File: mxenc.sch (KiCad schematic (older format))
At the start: 28 parts, among them J4 Conn_01x06, J6 Conn_01x06, J8 Conn_01x06 DNP, SW1 SW_Push, SW2 SW_Push, U1 IMX8MM, U10 24LC16, Y2 Crystal_GND24

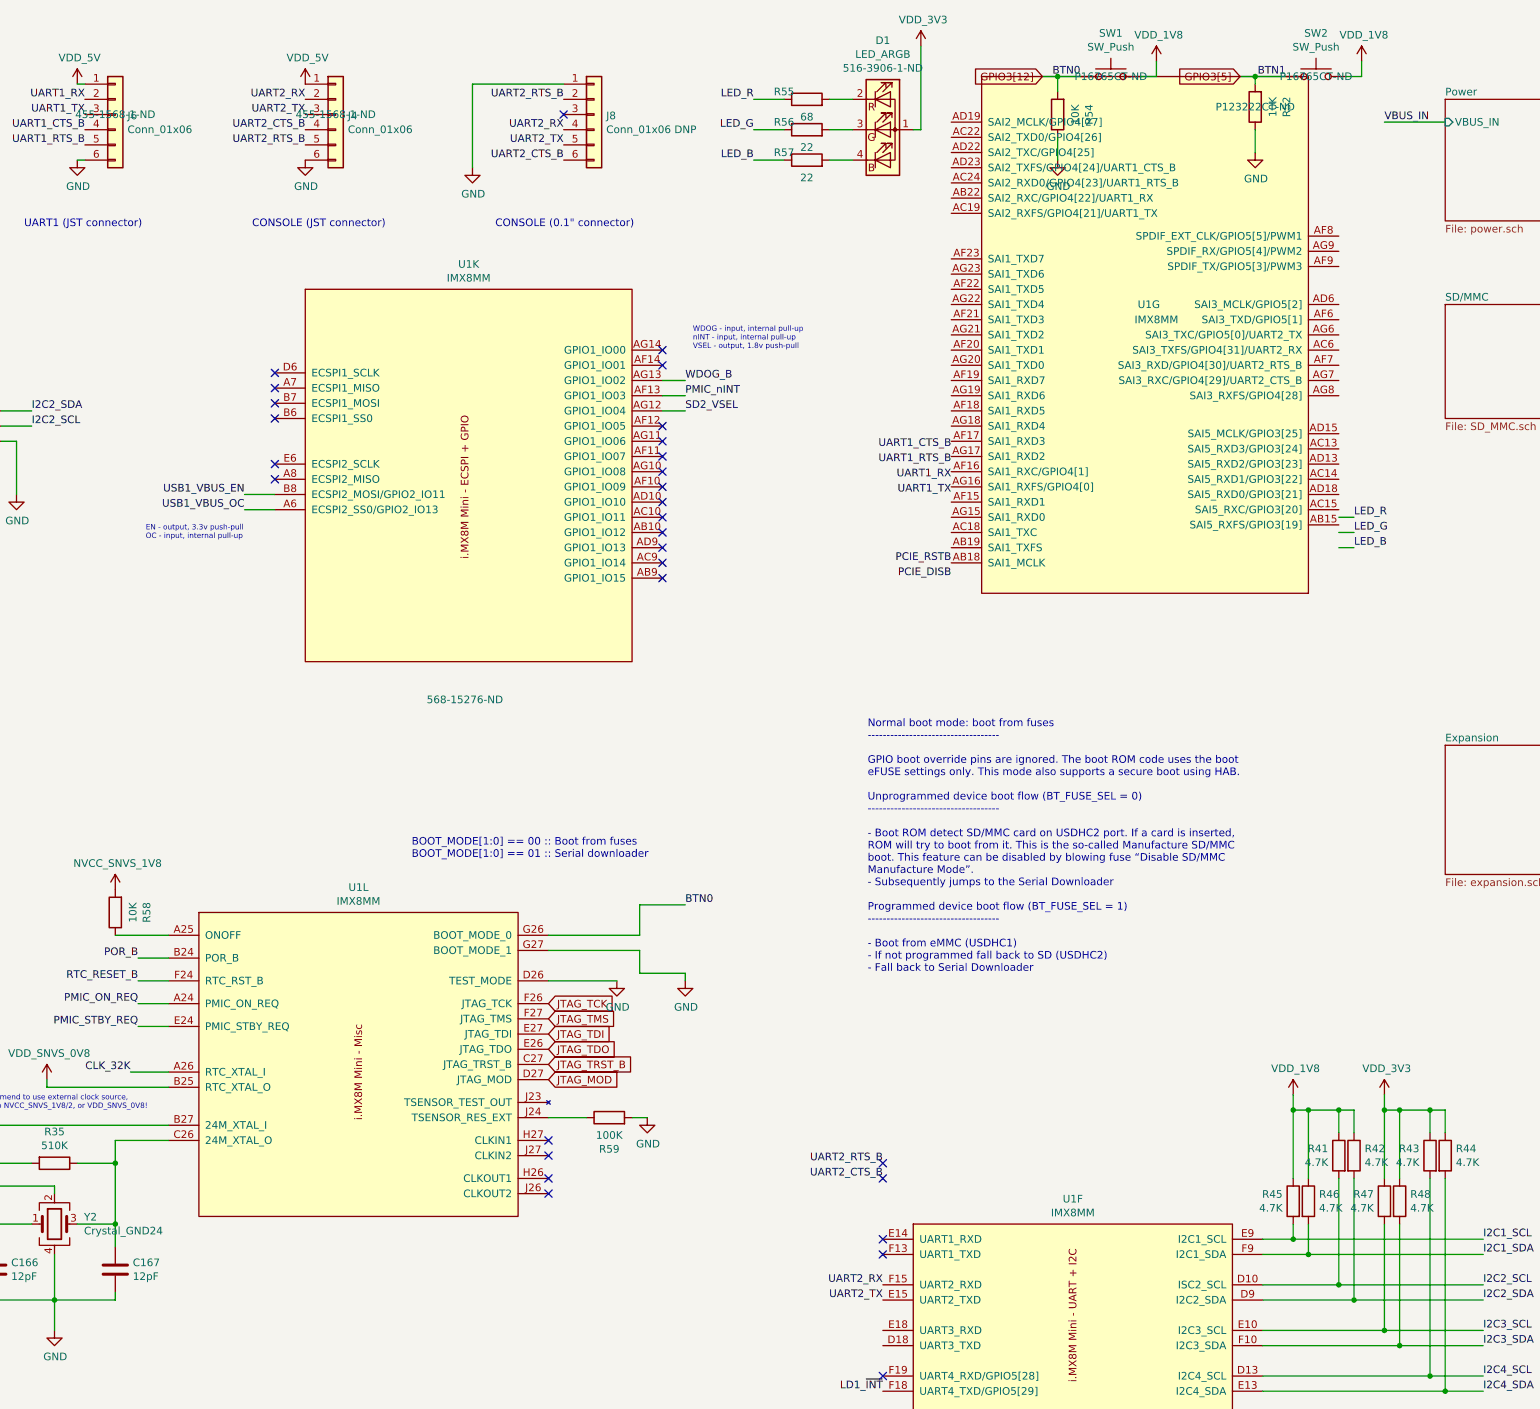
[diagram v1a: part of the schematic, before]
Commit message: add sai, mdio, sdhc to headers
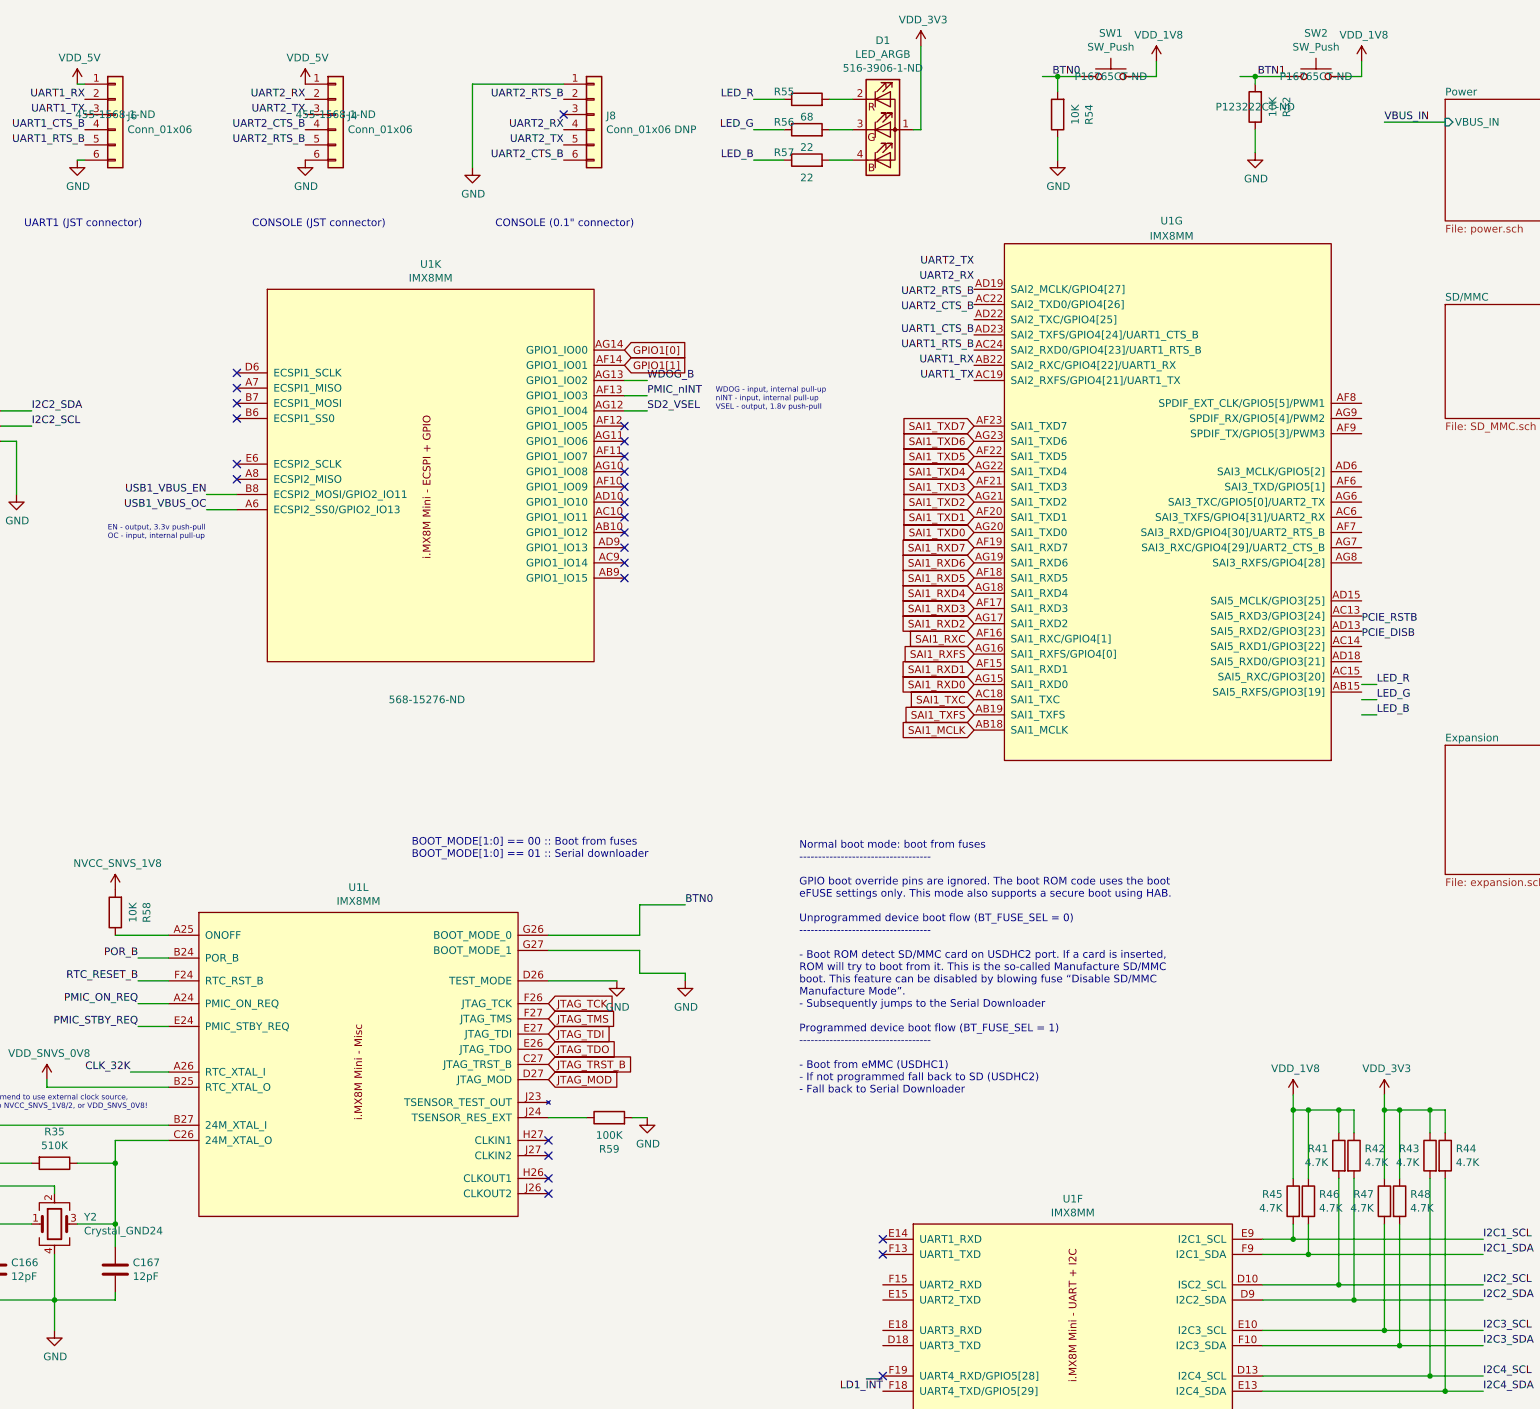
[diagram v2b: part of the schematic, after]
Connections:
- net labels added: GPIO1[0], GPIO1[1], SAI1_MCLK, SAI1_RXC, SAI1_RXD0, SAI1_RXD1, SAI1_RXD2, SAI1_RXD3, SAI1_RXD4, SAI1_RXD5, SAI1_RXD6, SAI1_RXD7, SAI1_RXFS, SAI1_TXC, SAI1_TXD0, SAI1_TXD1, SAI1_TXD2, SAI1_TXD3, SAI1_TXD4, SAI1_TXD5, SAI1_TXD6, SAI1_TXD7, SAI1_TXFS
- net labels removed: GPIO3[12], GPIO3[5]
- no-connect marks 32 -> 28
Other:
- moved on the sheet: U1G, U1K
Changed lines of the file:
@@
 L mxenc:MIMX8MM6DVTLZAA U1
 U 11 1 5DDE75DF
-P 4550 5250
-F 0 "U1" H 4575 8115 50  0000 C CNN
-F 1 "IMX8MM" H 4575 8024 50  0000 C CNN
-F 2 "mxenc:BGA-729_27x27_14.0x14.0mm" H 4800 8000 50  0001 C CNN
-F 3 "" H 3800 8000 50  0001 C CNN
-F 4 "568-15276-ND" H 4550 5250 50  0000 C CNN "Vendorpart"
-F 5 "NXP" H 4550 5250 50  0001 C CNN "Mfgr"
-F 6 "MIMX8MM6CVTKZAA" H 4550 5250 50  0001 C CNN "Part"
-	11   4550 5250
+P 4300 5250
+F 0 "U1" H 4325 8115 50  0000 C CNN
+F 1 "IMX8MM" H 4325 8024 50  0000 C CNN
+F 2 "mxenc:BGA-729_27x27_14.0x14.0mm" H 4550 8000 50  0001 C CNN
+F 3 "" H 3550 8000 50  0001 C CNN
+F 4 "568-15276-ND" H 4300 5250 50  0000 C CNN "Vendorpart"
+F 5 "NXP" H 4300 5250 50  0001 C CNN "Mfgr"
+F 6 "MIMX8MM6CVTKZAA" H 4300 5250 50  0001 C CNN "Part"
+	11   4300 5250
 	1    0    0    -1
 $EndComp
@@
 Text Label 13100 7400 2    50   ~ 0
 USB1_VBUS_EN
-Text Label 3100 3900 2    50   ~ 0
+Text Label 2850 3900 2    50   ~ 0
 USB1_VBUS_EN
 Text Label 13100 7300 2    50   ~ 0
 USB1_VBUS_OC
-Text Label 3100 4000 2    50   ~ 0
+Text Label 2850 4000 2    50   ~ 0
 USB1_VBUS_OC
 Wire Wire Line
-	3100 4000 3300 4000
-Wire Wire Line
-	3100 3900 3300 3900
+	2850 4000 3050 4000
+Wire Wire Line
+	2850 3900 3050 3900
 $Comp
 L mxenc:VDD_1V8 #PWR0246
@@
 L mxenc:MIMX8MM6DVTLZAA U1
 U 7 1 5D8D5047
-P 9050 1850
-F 0 "U1" H 9050 2650 50  0000 C CNN
-F 1 "IMX8MM" H 9000 2750 50  0000 C CNN
-F 2 "mxenc:BGA-729_27x27_14.0x14.0mm" H 9300 4600 50  0001 C CNN
-F 3 "" H 8300 4600 50  0001 C CNN
-F 4 "NXP" H 9050 1850 50  0001 C CNN "Mfgr"
-F 5 "MIMX8MM6CVTKZAA" H 9050 1850 50  0001 C CNN "Part"
-F 6 "568-15276-ND" H 9050 1850 50  0001 C CNN "Vendorpart"
-	7    9050 1850
+P 9200 2950
+F 0 "U1" H 9200 2100 50  0000 C CNN
+F 1 "IMX8MM" H 9200 2200 50  0000 C CNN
+F 2 "mxenc:BGA-729_27x27_14.0x14.0mm" H 9450 5700 50  0001 C CNN
+F 3 "" H 8450 5700 50  0001 C CNN
+F 4 "NXP" H 9200 2950 50  0001 C CNN "Mfgr"
+F 5 "MIMX8MM6CVTKZAA" H 9200 2950 50  0001 C CNN "Part"
+F 6 "568-15276-ND" H 9200 2950 50  0001 C CNN "Vendorpart"
+	7    9200 2950
 	-1   0    0    1
 $EndComp
 Wire Wire Line
-	10300 4250 10400 4250
-Wire Wire Line
-	10300 4150 10400 4150
+	10450 5350 10550 5350
+Wire Wire Line
+	10450 5250 10550 5250
 $Comp
 L mxenc:VDD_3V3 #PWR0250
@@
 Wire Wire Line
 	6650 1300 6450 1300
-Text Label 10400 4050 0    50   ~ 0
+Text Label 10550 5150 0    50   ~ 0
 LED_R
-Text Label 10400 4150 0    50   ~ 0
+Text Label 10550 5250 0    50   ~ 0
 LED_G
-Text Label 10400 4250 0    50   ~ 0
+Text Label 10550 5350 0    50   ~ 0
 LED_B
 $Comp
@@
 $EndComp
 Wire Wire Line
-	10300 4050 10400 4050
+	10450 5150 10550 5150
 Text Label 6450 1300 2    50   ~ 0
 LED_R
@@
 Text Label 6450 1700 2    50   ~ 0
 LED_B
-Text Label 7300 9200 2    50   ~ 0
+Text Label 7900 2400 2    50   ~ 0
 UART2_TX
-Text Label 7300 9100 2    50   ~ 0
+Text Label 7900 2500 2    50   ~ 0
 UART2_RX
-Text Label 7300 8300 2    50   ~ 0
+Text Label 7900 2600 2    50   ~ 0
 UART2_RTS_B
-Text Label 7300 8400 2    50   ~ 0
+Text Label 7900 2700 2    50   ~ 0
 UART2_CTS_B
-Text Label 7750 3900 2    50   ~ 0
+Text Label 7900 3150 2    50   ~ 0
 UART1_TX
-Text Label 7750 3800 2    50   ~ 0
+Text Label 7900 3050 2    50   ~ 0
 UART1_RX
-Text Label 7750 3700 2    50   ~ 0
+Text Label 7900 2950 2    50   ~ 0
 UART1_RTS_B
-Text Label 7750 3600 2    50   ~ 0
+Text Label 7900 2850 2    50   ~ 0
 UART1_CTS_B
 Text Label 2050 1400 2    50   ~ 0
@@
 Wire Wire Line
 	4600 1200 5200 1200
-NoConn ~ 5850 2950
-NoConn ~ 5850 3050
-NoConn ~ 5850 3550
-NoConn ~ 5850 3650
-NoConn ~ 5850 3950
-NoConn ~ 5850 4050
-NoConn ~ 5850 4150
-NoConn ~ 5850 4250
-NoConn ~ 5850 4350
-NoConn ~ 5850 4450
-NoConn ~ 3300 3800
-NoConn ~ 3300 3700
-NoConn ~ 3300 3400
-NoConn ~ 3300 3300
-NoConn ~ 3300 3200
-NoConn ~ 3300 3100
+NoConn ~ 5600 3550
+NoConn ~ 5600 3650
+NoConn ~ 5600 3950
+NoConn ~ 5600 4050
+NoConn ~ 5600 4150
+NoConn ~ 5600 4250
+NoConn ~ 5600 4350
+NoConn ~ 5600 4450
+NoConn ~ 3050 3800
+NoConn ~ 3050 3700
+NoConn ~ 3050 3400
+NoConn ~ 3050 3300
+NoConn ~ 3050 3200
+NoConn ~ 3050 3100
 Wire Wire Line
 	2000 1200 2050 1200
@@
 Wire Wire Line
 	13050 4550 13350 4550
-Text Label 6000 3150 0    50   ~ 0
+Text Label 5750 3150 0    50   ~ 0
 WDOG_B
 Wire Wire Line
-	6000 3150 5850 3150
+	5750 3150 5600 3150
 Text Label 13050 4650 2    50   ~ 0
 PMIC_ON_REQ
@@
 Wire Wire Line
 	15550 4350 15400 4350
-Text Label 6000 3250 0    50   ~ 0
+Text Label 5750 3250 0    50   ~ 0
 PMIC_nINT
 Wire Wire Line
-	6000 3250 5850 3250
-NoConn ~ 5850 3450
+	5750 3250 5600 3250
+NoConn ~ 5600 3450
 Text Label 13050 4150 2    50   ~ 0
 SD2_VSEL
 Wire Wire Line
 	13050 4150 13350 4150
-Text Label 6000 3350 0    50   ~ 0
+Text Label 5750 3350 0    50   ~ 0
 SD2_VSEL
 Wire Wire Line
-	5850 3350 6000 3350
+	5600 3350 5750 3350
 Text Label 13000 6100 2    50   ~ 0
 PCIE_RSTB
@@
 Wire Wire Line
 	13000 6200 13350 6200
-Text Label 7750 4350 2    50   ~ 0
+Text Label 10450 4750 0    50   ~ 0
 PCIE_RSTB
-Text Label 7750 4450 2    50   ~ 0
+Text Label 10450 4850 0    50   ~ 0
 PCIE_DISB
 Text Label 13100 6850 2    50   ~ 0
@@
 Text Notes 4200 6300 0    50   ~ 0
 BOOT_MODE[1:0] == 00 :: Boot from fuses\nBOOT_MODE[1:0] == 01 :: Serial downloader
-Text Notes 7200 7050 0    50   ~ 0
+Text Notes 6750 7850 0    50   ~ 0
 Normal boot mode: boot from fuses\n-----------------------------------\n\nGPIO boot override pins are ignored. The boot ROM code uses the boot \neFUSE settings only. This mode also supports a secure boot using HAB.\n\nUnprogrammed device boot flow (BT_FUSE_SEL = 0)\n-----------------------------------\n\n- Boot ROM detect SD/MMC card on USDHC2 port. If a card is inserted, \nROM will try to boot from it. This is the so-called Manufacture SD/MMC\nboot. This feature can be disabled by blowing fuse “Disable SD/MMC \nManufacture Mode”.\n- Subsequently jumps to the Serial Downloader\n\nProgrammed device boot flow (BT_FUSE_SEL = 1)\n-----------------------------------\n\n- Boot from eMMC (USDHC1)\n- If not programmed fall back to SD (USDHC2)\n- Fall back to Serial Downloader
 Text Label 6000 6600 0    50   ~ 0
 BTN0
-Text Notes 2450 4200 0    35   ~ 0
+Text Notes 2200 4200 0    35   ~ 0
 EN - output, 3.3v push-pull\nOC - input, internal pull-up
-Text Notes 6050 2950 0    35   ~ 0
+Text Notes 6200 3350 0    35   ~ 0
 WDOG - input, internal pull-up\nnINT - input, internal pull-up\nVSEL - output, 1.8v push-pull
 Wire Wire Line
@@
 F1 "expansion.sch" 50
 $EndSheet
-NoConn ~ 7300 8300
-NoConn ~ 7300 8400
 Wire Wire Line
 	5550 7100 5100 7100
@@
 Text GLabel 5100 7750 2    50   Input ~ 0
 JTAG_MOD
-Text GLabel 8350 1150 0    50   Input ~ 0
-GPIO3[12]
 Wire Wire Line
 	8350 1150 8450 1150
@@
 Text Label 9950 1150 2    50   ~ 0
 BTN1
-Text GLabel 9650 1150 0    50   Input ~ 0
-GPIO3[5]
 Wire Wire Line
 	9650 1150 9750 1150
@@
 Wire Wire Line
 	9750 1150 9950 1150
-NoConn ~ 5850 3750
-NoConn ~ 5850 3850
+NoConn ~ 5600 3750
+NoConn ~ 5600 3850
 $Comp
 L Switch:SW_Push SW2
@@
 	1    0    0    -1
 $EndComp
+Text GLabel 5600 2950 2    50   Input ~ 0
+GPIO1[0]
+Text GLabel 5600 3050 2    50   Input ~ 0
+GPIO1[1]
+Text GLabel 7900 3450 0    50   Input ~ 0
+SAI1_TXD7
+Text GLabel 7900 3550 0    50   Input ~ 0
+SAI1_TXD6
+Text GLabel 7900 3650 0    50   Input ~ 0
+SAI1_TXD5
+Text GLabel 7900 3750 0    50   Input ~ 0
+SAI1_TXD4
+Text GLabel 7900 3850 0    50   Input ~ 0
+SAI1_TXD3
+Text GLabel 7900 3950 0    50   Input ~ 0
+SAI1_TXD2
+Text GLabel 7900 4050 0    50   Input ~ 0
+SAI1_TXD1
+Text GLabel 7900 4150 0    50   Input ~ 0
+SAI1_TXD0
+Text GLabel 7900 4250 0    50   Input ~ 0
+SAI1_RXD7
+Text GLabel 7900 4350 0    50   Input ~ 0
+SAI1_RXD6
+Text GLabel 7900 4450 0    50   Input ~ 0
+SAI1_RXD5
+Text GLabel 7900 4550 0    50   Input ~ 0
+SAI1_RXD4
+Text GLabel 7900 4650 0    50   Input ~ 0
+SAI1_RXD3
+Text GLabel 7900 4750 0    50   Input ~ 0
+SAI1_RXD2
+Text GLabel 7900 4850 0    50   Input ~ 0
+SAI1_RXC
+Text GLabel 7900 4950 0    50   Input ~ 0
+SAI1_RXFS
+Text GLabel 7900 5050 0    50   Input ~ 0
+SAI1_RXD1
+Text GLabel 7900 5150 0    50   Input ~ 0
+SAI1_RXD0
+Text GLabel 7900 5250 0    50   Input ~ 0
+SAI1_TXC
+Text GLabel 7900 5350 0    50   Input ~ 0
+SAI1_TXFS
+Text GLabel 7900 5450 0    50   Input ~ 0
+SAI1_MCLK
 $EndSCHEMATC

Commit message: Ground mounting pads and route ecspi to expansion
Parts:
- J4, J6: symbol Connector_Generic:Conn_01x06 -> mxenc:JST-GH-6
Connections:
- net labels added: ECSPI1_MISO, ECSPI1_MOSI, ECSPI1_SCLK, ECSPI1_SS0, ECSPI2_MISO, ECSPI2_MOSI, ECSPI2_SCLK, ECSPI2_SS0, USB2_OC, USB2_OTG_OC, USB2_OTG_PWR, USB2_PWR_EN
- net labels removed: USB1_VBUS_EN, USB1_VBUS_OC
- wire segments 151 -> 149
- no-connect marks 28 -> 19
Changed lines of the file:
@@
 $EndComp
 $Comp
-L Connector_Generic:Conn_01x06 J6
+L mxenc:JST-GH-6 J6
 U 1 1 5CB89AB0
 P 2250 1400
@@
 F2 "LD1_~INT" I L 13350 6850 50
 F3 "USB1_VBUS_IN" O L 13350 6950 50
-F4 "USB1_VBUS_OC" O L 13350 7300 50
-F5 "USB1_VBUS_EN" I L 13350 7400 50
-F6 "DP_IRQ" O R 15400 6900 50
-F7 "DP_EN" I R 15400 7000 50
-F8 "DP_SCL" I R 15400 7100 50
-F9 "DP_SDA" B R 15400 7200 50
-F10 "USB2_SCL" I R 15400 7350 50
-F11 "USB2_SDA" B R 15400 7450 50
-F12 "USB1_PWR_SDA" B R 15400 7700 50
-F13 "USB1_PWR_SCL" I R 15400 7600 50
-F14 "DP_SUSP" I L 13350 7600 50
+F4 "DP_IRQ" O R 15400 6900 50
+F5 "DP_EN" I R 15400 7000 50
+F6 "DP_SCL" I R 15400 7100 50
+F7 "DP_SDA" B R 15400 7200 50
+F8 "USB2_SCL" I R 15400 7350 50
+F9 "USB2_SDA" B R 15400 7450 50
+F10 "USB1_PWR_SDA" B R 15400 7700 50
+F11 "USB1_PWR_SCL" I R 15400 7600 50
+F12 "DP_SUSP" I L 13350 7600 50
 $EndSheet
 $Sheet
@@
 $EndComp
 Wire Wire Line
-	13100 7300 13350 7300
-Wire Wire Line
-	13100 7400 13350 7400
-Text Label 13100 7400 2    50   ~ 0
-USB1_VBUS_EN
-Text Label 2850 3900 2    50   ~ 0
-USB1_VBUS_EN
-Text Label 13100 7300 2    50   ~ 0
-USB1_VBUS_OC
-Text Label 2850 4000 2    50   ~ 0
-USB1_VBUS_OC
-Wire Wire Line
-	2850 4000 3050 4000
-Wire Wire Line
-	2850 3900 3050 3900
+	6150 4900 6400 4900
+Wire Wire Line
+	6150 5000 6400 5000
 $Comp
 L mxenc:VDD_1V8 #PWR0246
@@
 LED_B
 $Comp
-L Connector_Generic:Conn_01x06 J4
+L mxenc:JST-GH-6 J4
 U 1 1 5DBDD2F9
 P 3700 1400
@@
 NoConn ~ 5600 3650
 NoConn ~ 5600 3950
-NoConn ~ 5600 4050
 NoConn ~ 5600 4150
 NoConn ~ 5600 4250
-NoConn ~ 5600 4350
-NoConn ~ 5600 4450
-NoConn ~ 3050 3800
-NoConn ~ 3050 3700
-NoConn ~ 3050 3400
-NoConn ~ 3050 3300
-NoConn ~ 3050 3200
-NoConn ~ 3050 3100
 Wire Wire Line
 	2000 1200 2050 1200
@@
 Text Label 6000 6600 0    50   ~ 0
 BTN0
-Text Notes 2200 4200 0    35   ~ 0
+Text Notes 5700 4700 0    35   ~ 0
 EN - output, 3.3v push-pull\nOC - input, internal pull-up
 Text Notes 6200 3350 0    35   ~ 0
@@
 Text GLabel 7900 5450 0    50   Input ~ 0
 SAI1_MCLK
+Text GLabel 8350 1150 0    50   Input ~ 0
+BTN0
+Text GLabel 9650 1150 0    50   Input ~ 0
+BTN1
+Text Label 5600 4350 0    50   ~ 0
+USB2_OTG_PWR
+Text Label 5600 4450 0    50   ~ 0
+USB2_OTG_OC
+Text Label 6150 5000 2    50   ~ 0
+USB2_OTG_PWR
+Text Label 6150 4900 2    50   ~ 0
+USB2_OTG_OC
+Text GLabel 6400 4900 2    50   Input ~ 0
+USB2_OC
+Text GLabel 6400 5000 2    50   Input ~ 0
+USB2_PWR_EN
+Text GLabel 3050 3700 0    50   Input ~ 0
+ECSPI2_SCLK
+Text GLabel 3050 3800 0    50   Input ~ 0
+ECSPI2_MISO
+Text GLabel 3050 3900 0    50   Input ~ 0
+ECSPI2_MOSI
+Text GLabel 3050 4000 0    50   Input ~ 0
+ECSPI2_SS0
+Text GLabel 3050 3100 0    50   Input ~ 0
+ECSPI1_SCLK
+Text GLabel 3050 3200 0    50   Input ~ 0
+ECSPI1_MISO
+Text GLabel 3050 3300 0    50   Input ~ 0
+ECSPI1_MOSI
+Text GLabel 3050 3400 0    50   Input ~ 0
+ECSPI1_SS0
+$Comp
+L power:GND #PWR?
+U 1 1 5F2A80D8
+P 2400 1450
+F 0 "#PWR?" H 2400 1200 50  0001 C CNN
+F 1 "GND" H 2405 1277 50  0000 C CNN
+F 2 "" H 2400 1450 50  0001 C CNN
+F 3 "" H 2400 1450 50  0001 C CNN
+	1    2400 1450
+	1    0    0    -1
+$EndComp
+$Comp
+L power:GND #PWR?
+U 1 1 5F2A97FE
+P 3850 1450
+F 0 "#PWR?" H 3850 1200 50  0001 C CNN
+F 1 "GND" H 3855 1277 50  0000 C CNN
+F 2 "" H 3850 1450 50  0001 C CNN
+F 3 "" H 3850 1450 50  0001 C CNN
+	1    3850 1450
+	1    0    0    -1
+$EndComp
 $EndSCHEMATC
